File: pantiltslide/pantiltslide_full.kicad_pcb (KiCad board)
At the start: 2 copper layers, 141 x 140 mm, 20 parts

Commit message: pcb updates
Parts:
- removed 24v in: TerminalBlock_MaiXu_MX126-5.0-02P_1x02_P5.00mm, TerminalBlock:TerminalBlock_MaiXu_MX126-5.0-02P_1x02_P5.00mm
- removed 5V in: TerminalBlock_MaiXu_MX126-5.0-02P_1x02_P5.00mm, TerminalBlock:TerminalBlock_MaiXu_MX126-5.0-02P_1x02_P5.00mm
- removed Motor 1: JST_XH_B4B-XH-A_1x04_P2.50mm_Vertical, Connector_JST:JST_XH_B4B-XH-A_1x04_P2.50mm_Vertical (x3)
- removed the REF** at (218.8, 67.0)
- removed the REF** at (150.0, 57.0)
- removed the REF** at (175.0, 67.5)
- removed the REF** at (175.0, 57.0)
- removed the REF** at (175.0, 77.5)
- removed the REF** at (164.0, 56.9)
- removed the REF** at (218.8, 57.0)
- removed the REF** at (175.0, 87.5)
- removed TMC0R (x3), tmc0L (x3): PinSocket_1x08_P2.54mm_Vertical, Connector_PinSocket_2.54mm:PinSocket_1x08_P2.54mm_Vertical
- added J17: Motor_Slide, Connector_PinHeader_2.54mm:PinHeader_1x04_P2.54mm_Vertical, F.Cu at (116.3, 132.3)
- added J18: Motor_Pan, Connector_PinHeader_2.54mm:PinHeader_1x04_P2.54mm_Vertical, F.Cu at (120.9, 132.3)
- added J19: Motor_Tilt, Connector_PinHeader_2.54mm:PinHeader_1x04_P2.54mm_Vertical, F.Cu at (125.5, 132.3)
- added J20: TCA9548A_Mux, Connector_PinSocket_2.54mm:PinSocket_1x08_P2.54mm_Vertical, F.Cu at (166.8, 132.3)
- added J21: AS5600_Pan, Connector_PinHeader_2.54mm:PinHeader_1x04_P2.54mm_Vertical, F.Cu at (130.1, 132.3)
- added J22: AS5600_Tilt, Connector_PinHeader_2.54mm:PinHeader_1x04_P2.54mm_Vertical, F.Cu at (134.7, 132.3)
- added J23: OLED, Connector_PinHeader_2.54mm:PinHeader_1x04_P2.54mm_Vertical, F.Cu at (139.2, 132.3)
- added J28: Motor_Aux, Connector_PinHeader_2.54mm:PinHeader_1x04_P2.54mm_Vertical, F.Cu at (143.8, 132.3)
- added J29: Enc_Slide, Connector_PinHeader_2.54mm:PinHeader_1x04_P2.54mm_Vertical, F.Cu at (148.4, 132.3)
- added J30: Enc_Pan, Connector_PinHeader_2.54mm:PinHeader_1x04_P2.54mm_Vertical, F.Cu at (153.0, 132.3)
- added J31: Enc_Tilt, Connector_PinHeader_2.54mm:PinHeader_1x04_P2.54mm_Vertical, F.Cu at (157.6, 132.3)
- added J32: Enc_Aux, Connector_PinHeader_2.54mm:PinHeader_1x04_P2.54mm_Vertical, F.Cu at (162.2, 132.3)
- added U1: tmc2209, TMC2209:TMC2209_SilentStepStick_Socket_18P, F.Cu at (116.4, 102.4)
- added U2: tmc2209, TMC2209:TMC2209_SilentStepStick_Socket_18P, F.Cu at (134.0, 102.4)
- added U3: tmc2209, TMC2209:TMC2209_SilentStepStick_Socket_18P, F.Cu at (151.5, 102.4)
- added U4: tmc2209, TMC2209:TMC2209_SilentStepStick_Socket_18P, F.Cu at (169.1, 102.4)
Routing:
- net (no net): track 658.2 -> 0.50 mm, vias 3 -> 0
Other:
- board text removed: "Dir"

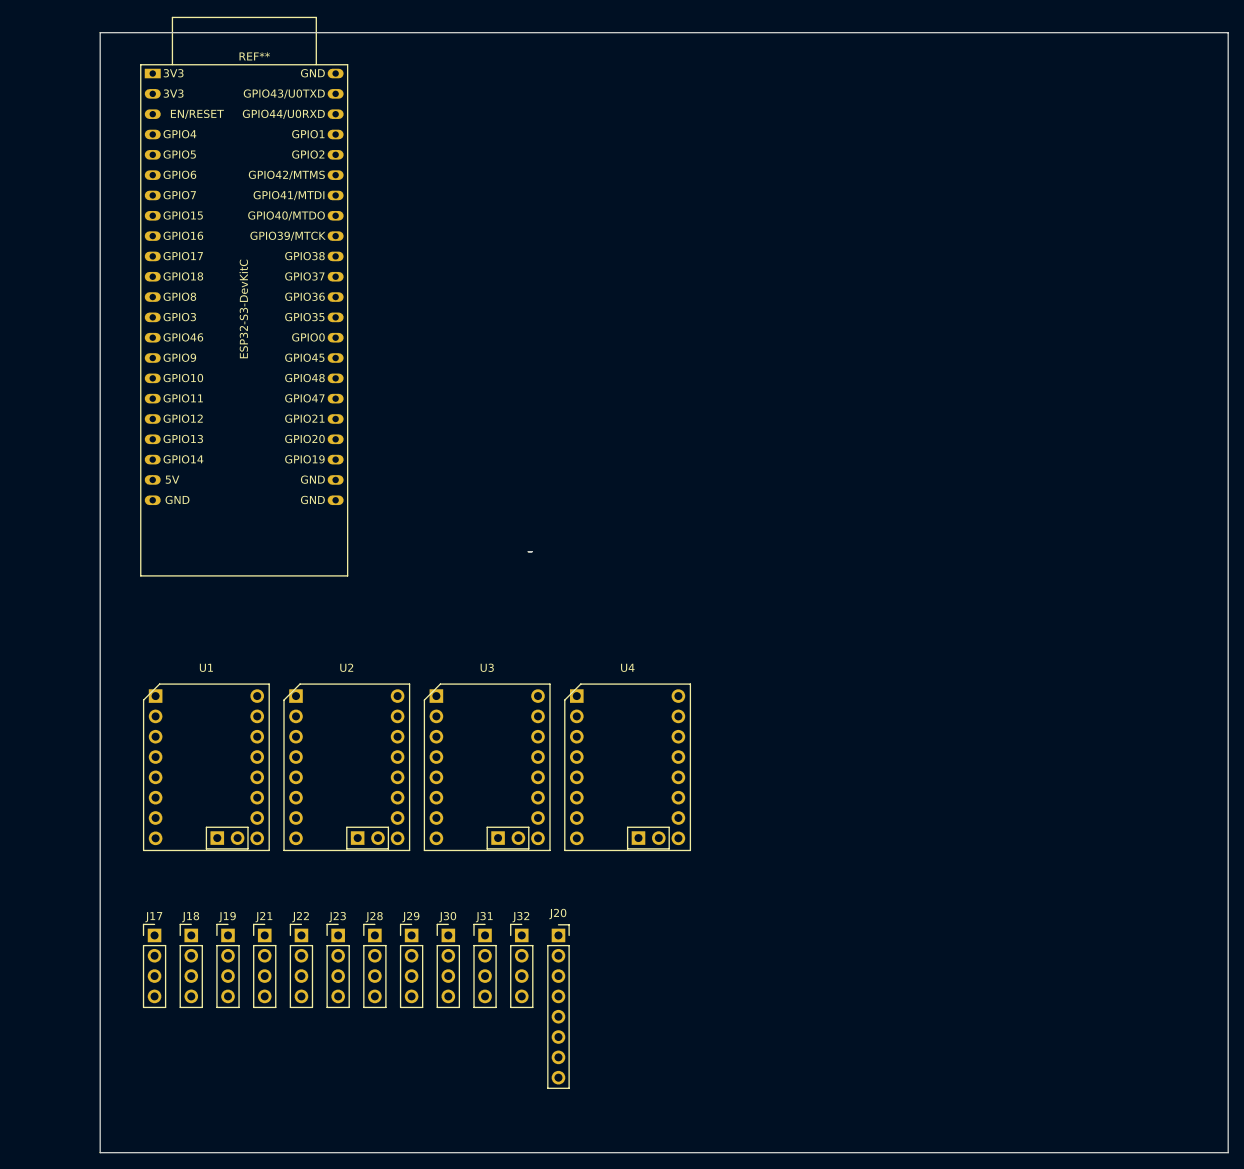
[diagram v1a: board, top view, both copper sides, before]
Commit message: fullpcb filled out
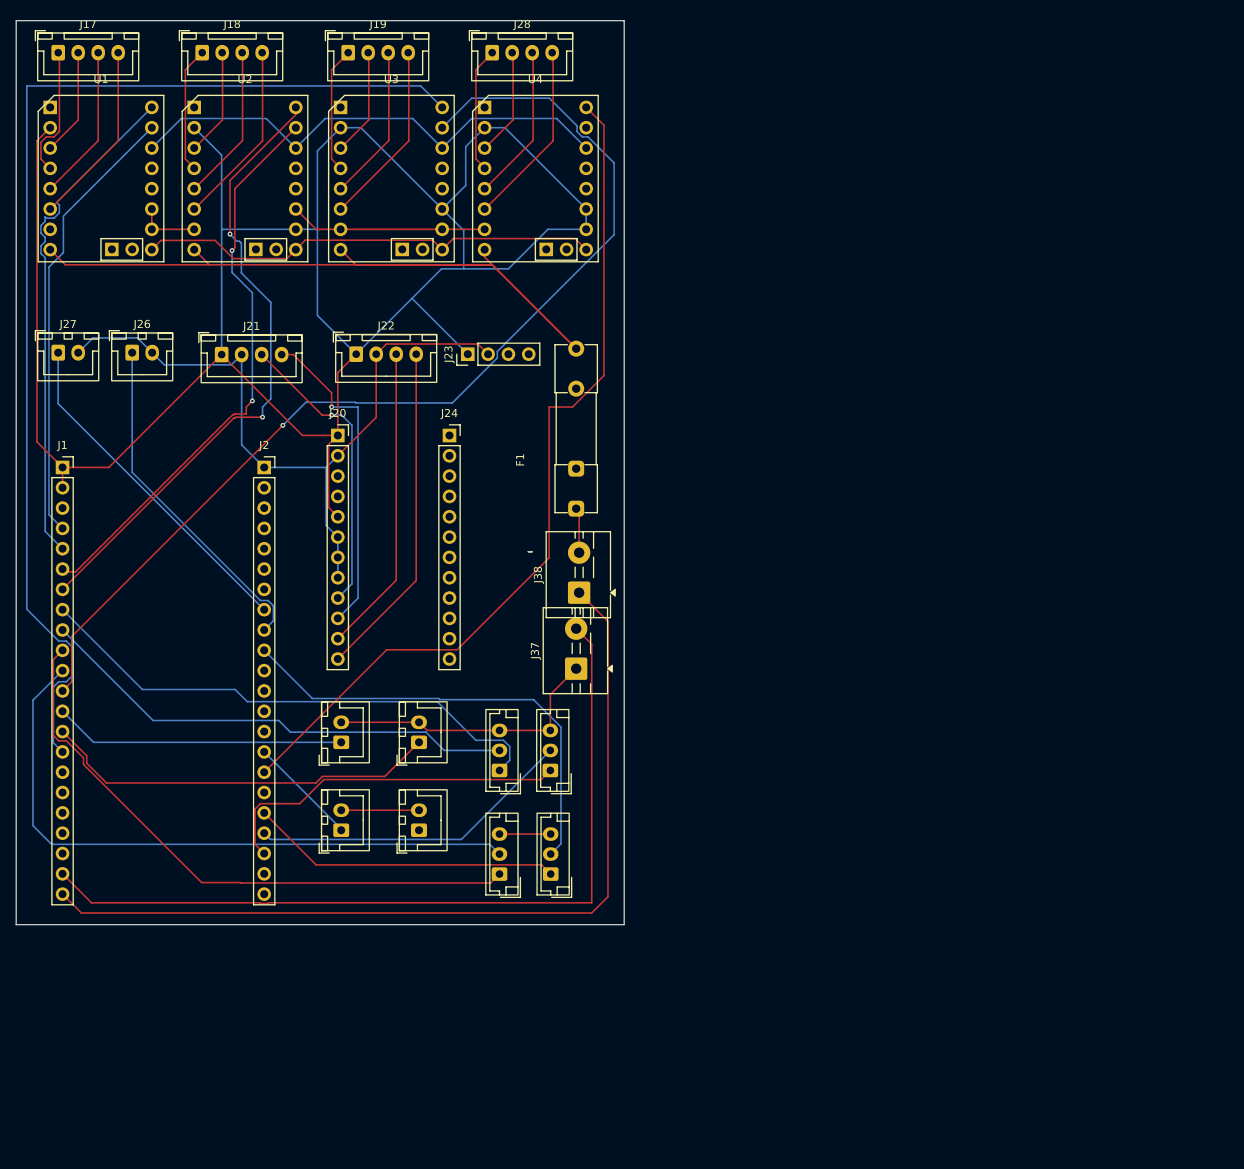
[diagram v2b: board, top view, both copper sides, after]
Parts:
- removed REF**: ESP32-S3-DevKitC, PCM_Espressif:ESP32-S3-DevKitC
- added F1: Fuse, Fuse:Fuseholder_Clip-5x20mm_Littelfuse_111_Inline_P20.00x5.00mm_D1.05mm_Horizontal, F.Cu at (169.0, 79.0)
- added J1: Conn_01x22_Socket, Connector_PinSocket_2.54mm:PinSocket_1x22_P2.54mm_Vertical, F.Cu at (104.8, 73.8)
- added J2: Conn_01x22_Socket, Connector_PinSocket_2.54mm:PinSocket_1x22_P2.54mm_Vertical, F.Cu at (130.0, 73.8)
- added J24: TCA9548A_Mux, Connector_PinSocket_2.54mm:PinSocket_1x12_P2.54mm_Vertical, F.Cu at (153.2, 69.8)
- added J26: Limit_Min, Connector_JST:JST_XH_B2B-XH-A_1x02_P2.50mm_Vertical, F.Cu at (113.5, 59.5)
- added J27: Limit_Max, Connector_JST:JST_XH_B2B-XH-A_1x02_P2.50mm_Vertical, F.Cu at (104.2, 59.5)
- added J33: Btn_SetKeyframe, Connector_JST:JST_XH_B2B-XH-A_1x02_P2.50mm_Vertical, F.Cu at (149.4, 119.2)
- added J34: Btn_ClearKeyframe, Connector_JST:JST_XH_B2B-XH-A_1x02_P2.50mm_Vertical, F.Cu at (139.6, 108.2)
- added J35: Btn_PlayPause, Connector_JST:JST_XH_B2B-XH-A_1x02_P2.50mm_Vertical, F.Cu at (139.6, 119.2)
- added J36: Btn_Reset, Connector_JST:JST_XH_B2B-XH-A_1x02_P2.50mm_Vertical, F.Cu at (149.4, 108.2)
- added J37: 5V_In, TerminalBlock:TerminalBlock_MaiXu_MX126-5.0-02P_1x02_P5.00mm, F.Cu at (169.0, 99.0)
- added J38: 24V_In, TerminalBlock:TerminalBlock_MaiXu_MX126-5.0-02P_1x02_P5.00mm, F.Cu at (169.4, 89.5)
- J17, J18, J19, J21, J22, J28: footprint Connector_PinHeader_2.54mm:PinHeader_1x04_P2.54mm_Vertical -> Connector_JST:JST_XH_B4B-XH-A_1x04_P2.50mm_Vertical
- J20: footprint Connector_PinSocket_2.54mm:PinSocket_1x08_P2.54mm_Vertical -> Connector_PinSocket_2.54mm:PinSocket_1x12_P2.54mm_Vertical
- J29, J30, J31, J32: footprint Connector_PinHeader_2.54mm:PinHeader_1x04_P2.54mm_Vertical -> Connector_JST:JST_EH_B3B-EH-A_1x03_P2.50mm_Vertical
- moved J19 111.4 mm to (140.5, 22.0)
- moved J28 111.3 mm to (158.5, 22.0)
- moved J17 111.0 mm to (104.2, 22.0)
- moved J18 110.4 mm to (122.2, 22.0)
- moved U1 74.8 mm to (103.2, 28.8)
- moved U2 74.7 mm to (121.2, 28.8)
- moved U3 74.6 mm to (139.6, 28.8)
- moved U4 74.5 mm to (157.6, 28.8)
- moved J23 74.4 mm to (155.4, 59.7), turned to 90 degrees
- moved J22 73.0 mm to (141.5, 59.7)
- moved J21 72.8 mm to (124.7, 59.7)
- moved J20 68.3 mm to (139.2, 69.8)
- moved J29 23.4 mm to (159.4, 111.7), turned to 90 degrees
- moved J32 20.9 mm to (165.8, 111.7), turned to 90 degrees
- moved J31 11.2 mm to (165.8, 124.7), turned to 90 degrees
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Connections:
- J20 pad 5: MUX_CH0_SDA -> 3.3v
- J20 pad 6: MUX_CH0_SCL -> GND
- J20 pad 7: MUX_CH1_SDA -> GND
- J20 pad 8: MUX_CH1_SCL -> GND
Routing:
- net 3.3v: track 0.00 -> 289.4 mm
- net GND: track 0.00 -> 286.2 mm
- net GPIO_9: track 0.00 -> 141.1 mm
- net GPIO_8: track 0.00 -> 132.2 mm, vias 0 -> 1
- net +24V: track 0.00 -> 110.4 mm
- net GPIO_48: track 0.00 -> 108.5 mm
- net VCC_5V: track 0.00 -> 102.8 mm
- net GPIO_18: track 0.00 -> 80.7 mm
- net GPIO_7: track 0.00 -> 78.8 mm, vias 0 -> 2
- net GPIO_17: track 0.00 -> 75.5 mm
- net GPIO_6: track 0.00 -> 71.7 mm, vias 0 -> 2
- net GPIO_15: track 0.00 -> 66.5 mm
- net GPIO_5: track 0.00 -> 63.6 mm
- net GPIO_42: track 0.00 -> 63.5 mm
- net GPIO_16: track 0.00 -> 61.0 mm
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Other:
- board size 141 x 140 mm -> 76 x 113 mm
